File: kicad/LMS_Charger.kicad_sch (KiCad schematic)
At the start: 20 parts, among them J1 USB4105-GF-A-120, J2 Cable Pad, J3 Cable Pad, J4 Cable Pad, J5 Cable Pad, Q1 DMP2165UW, U1 MCP73833-AMI

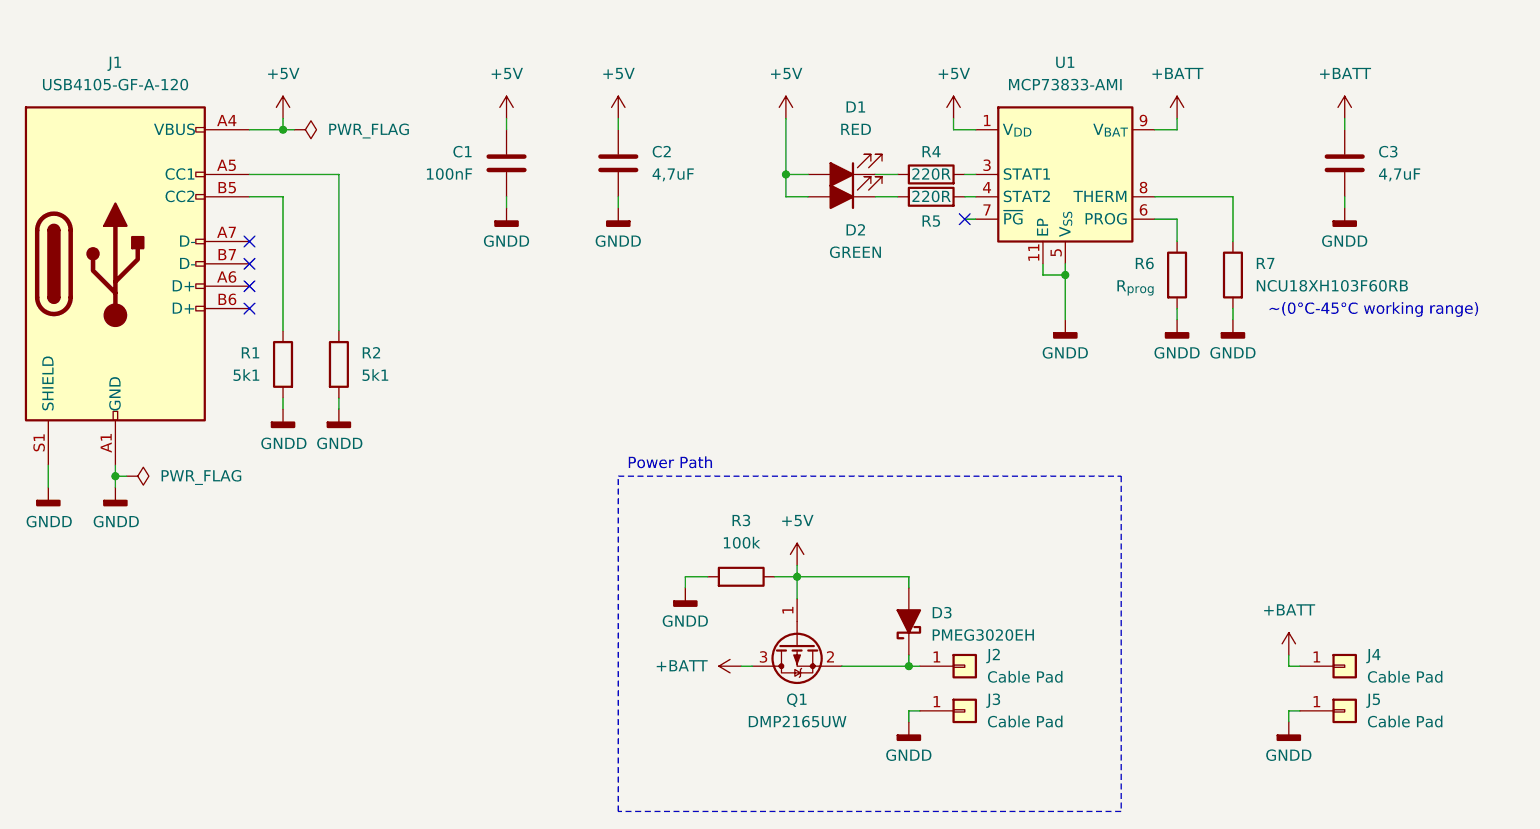
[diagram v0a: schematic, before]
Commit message: feat(lower_current): Created light version of charger for small bateries
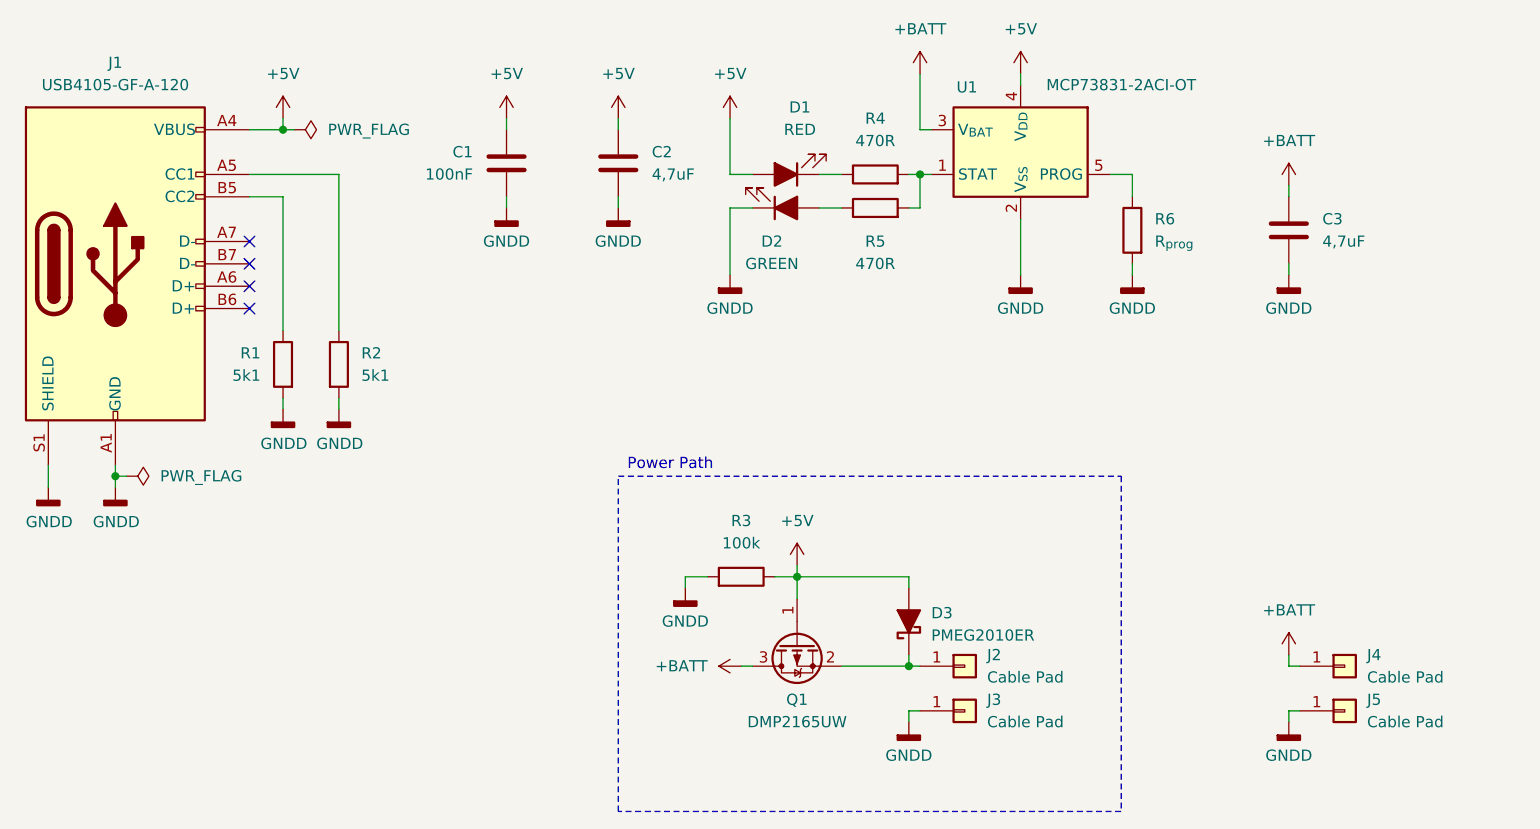
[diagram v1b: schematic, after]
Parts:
- removed R7: NCU18XH103F60RB, Resistor_SMD:R_0603_1608Metric, symbol Device:R
- removed U1: MCP73833-AMI, Package_DFN_QFN:DFN-10-1EP_3x3mm_P0.5mm_EP1.58x2.35mm, symbol Battery_Management:MCP73833-xxx-MF
- added U1: MCP73831-2ACI-OT, Package_TO_SOT_SMD:SOT-23-5, symbol Battery_Management:MCP73831-2-OT
- D3: value PMEG3020EH -> PMEG2010ER
- R4, R5: value 220R -> 470R
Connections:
- net +5V: now also U1.4 (V_{DD}); no longer D2.2 (A)
- net +BATT: now also U1.3 (V_{BAT})
- net GNDD: now also D2.1 (K), U1.2 (V_{SS})
- net at R5.1: now also D2.2 (A); no longer D2.1 (K)
- net at R5.2: now also R4.2, U1.1 (STAT)
- net at R6.1: now also U1.5 (PROG)
- no-connect marks 5 -> 4
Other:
- note removed: "~(0°C-45°C working range)"
- moved on the sheet: C3, D1, D2, R4, R5, R6

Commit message: fix(values): Minor updates in components and footprints
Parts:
- R6: value R_{prog} -> 2k2
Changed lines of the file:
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@@
 			)
 		)
-		(property "Value" "R_{prog}"
+		(property "Value" "2k2"
 			(at 187.96 74.9299 0)
 			(effects

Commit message: fix(power_path): Solved problem with leaking current through reverse diode, adjusted LED resistors
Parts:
- D3: value PMEG2010ER -> PMEG2010BER
- R4, R5: value 470R -> 1k
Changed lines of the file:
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@@
 (kicad_sch
-	(version 20231120)
+	(version 20250114)
 	(generator "eeschema")
-	(generator_version "8.0")
+	(generator_version "9.0")
 	(paper "A4")
 	(title_block
 		(title "LMS Charger")
-		(date "2024-08-22")
-		(rev "v0.2.0-L")
+		(date "2024-10-17")
+		(rev "v0.2.2")
 		(company "Petr Vilím")
 	)
+	(rectangle
+		(start 127 101.6)
+		(end 184.15 139.7)
+		(stroke
+			(width 0)
+			(type dash)
+		)
+		(fill
+			(type none)
+		)
+	)
+	(text "Power Path"
+		(exclude_from_sim no)
+		(at 128.016 100.33 0)
+		(effects
+			(font
+				(size 1.27 1.27)
+			)
+			(justify left)
+		)
+	)
 	(junction
 		(at 147.32 113.03)
@@
 		)
 	)
-	(rectangle
-		(start 127 101.6)
-		(end 184.15 139.7)
-		(stroke
-			(width 0)
-			(type dash)
-		)
-		(fill
-			(type none)
-		)
-	)
-	(text "Power Path"
-		(exclude_from_sim no)
-		(at 128.016 100.33 0)
-		(effects
-			(font
-				(size 1.27 1.27)
-			)
-			(justify left)
-		)
-	)
 	(symbol
 		(lib_id "Device:Q_PMOS_GSD")
@@
 			)
 		)
-		(property "Value" "470R"
+		(property "Value" "1k"
 			(at 156.21 77.47 90)
 			(effects
@@
 			)
 		)
-		(property "Value" "470R"
+		(property "Value" "1k"
 			(at 156.21 63.5 90)
 			(effects
@@
 			)
 		)
-		(property "Value" "PMEG2010ER"
+		(property "Value" "PMEG2010BER"
 			(at 162.56 119.6974 90)
 			(effects
@@
 		)
 	)
+	(embedded_fonts no)
 )
